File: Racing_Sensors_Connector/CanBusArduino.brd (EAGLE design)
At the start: 48.3 x 41.9 mm, 21 parts, among them U1 328P, Y1 16MHz

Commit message: Redesign PCB slightly
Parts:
- C1, C2: device SparkFun-Capacitors:0402 -> SparkFun-Capacitors:0603
- moved CANH/L 3.59 mm to (5.59, 36.2)
- moved PWR 3.59 mm to (5.59, 6.99)
- moved ADC0/1 3.26 mm to (5.59, 30.4)
- moved DIO 3.26 mm to (5.59, 12.8)
- moved ADC2/3 3.07 mm to (5.59, 24.5)
- moved ADC4/5 3.07 mm to (5.59, 18.7)
- turned R1 to 270 degrees
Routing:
- net RS: track 106.5 -> 100.8 mm
- net VCC: track 79.0 -> 73.5 mm
- net CANL: track 45.9 -> 41.0 mm
- net A3: track 19.1 -> 14.8 mm
- net CANH: track 41.5 -> 37.6 mm
- net D3: track 21.7 -> 18.1 mm
- net D4: track 38.0 -> 34.5 mm
- net A5: track 10.5 -> 7.26 mm
- net A4: track 14.1 -> 11.0 mm
- net A2: track 22.7 -> 20.0 mm
- net A1: track 27.1 -> 24.7 mm
- net A0: track 31.5 -> 29.3 mm
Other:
- board size 48.3 x 41.9 mm -> 48.3 x 43.2 mm

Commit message: Start redesign
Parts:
- removed C1, C2: 0.1uF, SparkFun-Capacitors:0603
- removed CAN_COMM: MCP2515, SparkFun-IC-Comms:DIP18
- removed CAP_2515_OSC1, CAP_2515_OSC2: 22pF, SparkFun-Capacitors:0603
- removed DIO: (no value), SparkFun-Connectors:MOLEX-1X2
- removed R1: 10k, SparkFun-Resistors:0603
- removed U1: 328P, SparkFun-IC-Microcontroller:DIP28
- removed Y1: 16MHz, SparkFun-Clocks:HC49US
- added ADC6/7, CANH/L2, I2C, TX/RX: (no value), SparkFun-Connectors:MOLEX-1X2
- added BYP1, BYP2: 0.1uF, SparkFun-Capacitors:0603
- added COSC1, COSC2: 22pF, SparkFun-Capacitors:0603
- added ISP: (no value), SparkFun-Connectors:2X3
- added OSC: 16MHz, SparkFun-Clocks:HC49US
- added RST_PULLUP, SD_PULLUP: 10k, SparkFun-Resistors:0603
- added U2: SPARKFUN_USD-SOCKETSMD, microSD-Breakout-v14:SPARKFUN_MICRO-SD-SOCKET-PP
- added U3: AT90CAN128-16AI, _hhn_at90can32_64_128_v2:TQFP64-0.8MM
- PRGM: value 455-1750-1-ND -> (none)
- moved PWR 37.5 mm to (43.0, 9.91), turned to 90 degrees
- moved R_2551_RS 7.62 mm to (30.5, 33.0)
- renumbered CANH/L to CANH/L1
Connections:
- removed net CAN_CS: CAN_COMM.16, U1.16
- removed net CAN_INT: CAN_COMM.12, U1.4
- removed net D3: DIO.2, U1.5
- removed net D4: DIO.1, U1.11
- removed net RS: CAN_COMM.17, PRGM.3, R1.2, U1.1
- new net A6: ADC6/7.1, U3.55
- new net A7: ADC6/7.2, U3.54
- new net RESET: ISP.5, PRGM.3, RST_PULLUP.1, U3.20
- new net RX1: TX/RX.2, U3.27
- new net SCL: I2C.2, U3.25
- new net SDA: I2C.1, U3.26
- new net SD_CD: SD_PULLUP.1, U2.CD2, U3.44
- new net SD_CS: U2.2, U3.45
- new net TX1: TX/RX.1, U3.28
- net A0: now also U3.61; no longer U1.23
- net A1: now also U3.60; no longer U1.24
- net A2: now also U3.59; no longer U1.25
- net A3: now also U3.58; no longer U1.26
- net A4: now also U3.57; no longer U1.27
- net A5: now also U3.56; no longer U1.28
- net CANH: now also CANH/L2.2
- net CANL: now also CANH/L2.1
- net CAN_RXD: now also U3.31; no longer CAN_COMM.2
- net CAN_TXD: now also U3.30; no longer CAN_COMM.1
- net GND: now also BYP1.2, BYP2.2, COSC1.2, COSC2.2, ISP.6, U2.6, U2.GND1, U2.GND2, U3.22, U3.53, U3.63; no longer C1.2, C2.2, CAN_COMM.9, CAP_2515_OSC1.2, CAP_2515_OSC2.2, U1.22, U1.8
- net MISO: now also ISP.1, U2.7, U3.13; no longer CAN_COMM.15, U1.18
- net MOSI: now also ISP.4, U2.3, U3.12; no longer CAN_COMM.14, U1.17
- net OSC1: now also COSC1.1, OSC.2, U3.24; no longer CAN_COMM.8, CAP_2515_OSC1.1, Y1.2
- net OSC2: now also COSC2.1, OSC.1, U3.23; no longer CAN_COMM.7, CAP_2515_OSC2.1, Y1.1
- net RX: now also U3.2; no longer U1.2
- net SCK: now also ISP.3, U2.5, U3.11; no longer CAN_COMM.13, U1.19
- net TX: now also U3.3; no longer U1.3
- net VCC: now also BYP1.1, BYP2.1, ISP.2, RST_PULLUP.2, SD_PULLUP.2, U2.4, U3.21, U3.52, U3.64; no longer C1.1, C2.1, CAN_COMM.18, R1.1, U1.20, U1.7
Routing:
- net RS: track 100.8 -> 0.00 mm
- net CAN_INT: track 75.8 -> 0.00 mm
- net RESET: track 0.00 -> 61.6 mm, vias 0 -> 1
- net CAN_CS: track 45.1 -> 0.00 mm
- net VCC: track 73.5 -> 117.6 mm, vias 0 -> 3
- net D4: track 34.5 -> 0.00 mm
- net A7: track 0.00 -> 32.0 mm, vias 0 -> 2
- net RX: track 3.81 -> 33.3 mm
- net RX1: track 0.00 -> 27.4 mm
- net A6: track 0.00 -> 26.5 mm, vias 0 -> 2
- net SCK: track 32.6 -> 56.3 mm, vias 0 -> 1
- net SCL: track 0.00 -> 22.7 mm
- net TX1: track 0.00 -> 20.6 mm
- net SDA: track 0.00 -> 20.5 mm, vias 0 -> 1
- net TX: track 3.81 -> 22.7 mm, vias 0 -> 1
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
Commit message: Before SD fix
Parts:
- removed CAN_INTERFACE: MCP2551-I/P, can_transceiver:DIP254P762X432-8
- removed R_2551_RS: 4.7k, SparkFun-Resistors:0603
- added IFACE: MCP2561-E/SN, Volks73-MicrochipTechnology:SOIC-8
- moved ISP 31.8 mm to (30.5, 2.54)
- moved I2C 30.7 mm to (34.3, 17.8), turned to 90 degrees
- moved BYP2 25.5 mm to (24.1, 5.08)
- moved ADC0/1 22.7 mm to (5.08, 7.62)
- moved PRGM 17.7 mm to (30.5, 7.62)
- moved COSC1 17.2 mm to (20.3, 38.1)
- moved COSC2 17.2 mm to (16.5, 38.1)
- moved OSC 17.2 mm to (7.62, 38.1)
- moved CANH/L2 16.9 mm to (34.3, 30.5)
- moved PWR 16.7 mm to (34.3, 24.1)
- moved BYP1 15.1 mm to (24.1, 26.7), turned to 180 degrees
- moved CAP_CANL 14.8 mm to (25.4, 30.5)
- moved R2 14.8 mm to (29.2, 30.5)
- moved ADC6/7 13.8 mm to (5.08, 26.7)
- moved U2 13.4 mm to (23.7, 16.8)
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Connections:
- removed net CI_RS: CAN_INTERFACE.8, R_2551_RS.2
- new net CAN_STBY: IFACE.8, U3.46
- net A0: now also ADC0/1.2; no longer ADC0/1.1
- net A1: now also ADC0/1.1; no longer ADC0/1.2
- net A2: now also ADC2/3.2; no longer ADC2/3.1
- net A3: now also ADC2/3.1; no longer ADC2/3.2
- net A4: now also ADC4/5.2; no longer ADC4/5.1
- net A5: now also ADC4/5.1; no longer ADC4/5.2
- net A6: now also ADC6/7.2; no longer ADC6/7.1
- net A7: now also ADC6/7.1; no longer ADC6/7.2
- net CANH: now also IFACE.7; no longer CAN_INTERFACE.7
- net CANL: now also IFACE.6; no longer CAN_INTERFACE.6
- net CAN_RXD: now also IFACE.4; no longer CAN_INTERFACE.4
- net CAN_TXD: now also IFACE.1; no longer CAN_INTERFACE.1
- net GND: now also IFACE.2; no longer CAN_INTERFACE.2, R_2551_RS.1
- net VCC: now also IFACE.3; no longer CAN_INTERFACE.3
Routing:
- net CAN_STBY: track 0.00 -> 49.1 mm
- net VCC: track 117.6 -> 69.6 mm, vias 3 -> 4
- net TX: track 22.7 -> 55.7 mm, vias 1 -> 0
- net RESET: track 61.6 -> 28.9 mm, vias 1 -> 0
- net RX: track 33.3 -> 60.8 mm
- net MISO: track 60.8 -> 34.2 mm
- net SCK: track 56.3 -> 34.2 mm
- net CANL: track 56.1 -> 36.2 mm, vias 0 -> 1
- net MOSI: track 53.6 -> 38.0 mm, vias 1 -> 3
- net A7: track 32.0 -> 17.2 mm, vias 2 -> 0
- net CAN_RXD: track 35.3 -> 24.7 mm, vias 0 -> 2
- net CANH: track 50.8 -> 40.3 mm
- net RX1: track 27.4 -> 17.8 mm
- net A6: track 26.5 -> 17.2 mm, vias 2 -> 0
- net CAN_TXD: track 24.8 -> 32.3 mm, vias 1 -> 2
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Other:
- board size 48.3 x 43.2 mm -> 39.4 x 40.6 mm
- board text added: "+"
- board text added: "7 6 5 4 3 2 1 0"
- board text added: "CAN Communicator WashU Racing 2018-19"
- board text added: "Connor Monahan"
- board text added: "H L"
- board text added: "L H"
- board text added: "RX1"
- board text added: "SCL"
- board text added: "SDA"
- board text added: "TX1"
- board text removed: "Design: Connor Monahan"
- board text removed: "Ethan Shry"
- board text removed: "WASHU RACING 2017-18"

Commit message: Teensy shield version
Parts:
- removed ADC0/1, ADC2/3, ADC4/5, ADC6/7, I2C, TX/RX: (no value), SparkFun-Connectors:MOLEX-1X2
- removed BYP2: 0.1uF, SparkFun-Capacitors:0603
- removed CAP_CANH, CAP_CANL: 560pF, SparkFun-Capacitors:0603
- removed COSC1, COSC2: 22pF, SparkFun-Capacitors:0603
- removed ISP: (no value), SparkFun-Connectors:2X3
- removed OSC: 16MHz, SparkFun-Clocks:HC49US
- removed PRGM: (no value), SparkFun-Connectors:1X03
- removed R2, R3: 100, SparkFun-Resistors:0603
- removed RST_PULLUP: 10k, SparkFun-Resistors:0603
- removed U3: AT90CAN128-16AI, _hhn_at90can32_64_128_v2:TQFP64-0.8MM
- added BT1: (no value), SparkFun-Batteries:BATTCON_20MM_4LEGS
- added CCANH, CCANL: 560pF, SparkFun-Capacitors:0603
- added RCANH, RCANL: 100, SparkFun-Resistors:0603
- added TEENSY: TEENSY_3.1-3.2_ALL_PINS, Teensy_3_and_LC_Series_Boards_v1.4:TEENSY_3.0-3.2&LC_ALL_PINS
- moved PWR 31.9 mm to (2.54, 26.7), turned to 270 degrees
- moved CANH/L2 25.3 mm to (10.2, 38.1), turned to 180 degrees
- moved IFACE 24.4 mm to (31.8, 12.7), flipped to the bottom
- moved BYP1 20.5 mm to (31.8, 7.62), flipped to the bottom
- moved U2 17.5 mm to (6.22, 16.0), flipped to the top
- moved SD_PULLUP 15.9 mm to (12.7, 19.1), turned to 0 degrees
- moved CANH/L1 2.54 mm to (2.54, 33.0)
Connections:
- removed net A4: ADC4/5.2, U3.57
- removed net A5: ADC4/5.1, U3.56
- removed net OSC1: COSC1.1, OSC.2, U3.24
- removed net OSC2: COSC2.1, OSC.1, U3.23
- removed net RESET: ISP.5, PRGM.3, RST_PULLUP.1, U3.20
- removed net RX: PRGM.1, U3.2
- removed net TX: PRGM.2, U3.3
- new net 3.3V: SD_PULLUP.2, TEENSY.3.3V, TEENSY.3.3V1, U2.4
- new net 3V: BT1.POSITIVE@1, BT1.POSITIVE@2, BT1.POSITIVE@3, BT1.POSITIVE@4, TEENSY.VBAT
- new net A8: TEENSY.22/A8
- new net A9: TEENSY.23/A9
- new net AREF: TEENSY.AREF
- new net VUSB: TEENSY.VUSB
- net A0: now also TEENSY.14/A0; no longer ADC0/1.2, U3.61
- net A1: now also TEENSY.15/A1; no longer ADC0/1.1, U3.60
- net A2: now also TEENSY.16/A2; no longer ADC2/3.2, U3.59
- net A3: now also TEENSY.17/A3; no longer ADC2/3.1, U3.58
- net A6: now also TEENSY.20/A6; no longer ADC6/7.2, U3.55
- net A7: now also TEENSY.21/A7; no longer ADC6/7.1, U3.54
- net CANH: now also RCANH.2; no longer R3.2
- net CANL: now also RCANL.2; no longer R2.2
- net CAN_RXD: now also TEENSY.4; no longer U3.31
- net CAN_STBY: now also TEENSY.5; no longer U3.46
- net CAN_TXD: now also TEENSY.3; no longer U3.30
- net GND: now also BT1.NEGATIVE, CCANH.2, CCANL.1, TEENSY.AGND, TEENSY.GND, TEENSY.GND1; no longer BYP2.2, CAP_CANH.2, CAP_CANL.1, COSC1.2, COSC2.2, ISP.6, U3.22, U3.53, U3.63
- net MISO: now also TEENSY.12; no longer ISP.1, U3.13
- net MOSI: now also TEENSY.11; no longer ISP.4, U3.12
- net N$6: now also CCANL.2, RCANL.1; no longer CAP_CANL.2, R2.1
- net N$7: now also CCANH.1, RCANH.1; no longer CAP_CANH.1, R3.1
- net RX1: now also TEENSY.0; no longer TX/RX.2, U3.27
- net SCK: now also TEENSY.13; no longer ISP.3, U3.11
- net SCL: now also TEENSY.19/A5; no longer I2C.2, U3.25
- net SDA: now also TEENSY.18/A4; no longer I2C.1, U3.26
- net SD_CD: now also TEENSY.7; no longer U3.44
- net SD_CS: now also TEENSY.6; no longer U3.45
- net TX1: now also TEENSY.1; no longer TX/RX.1, U3.28
- net VCC: now also TEENSY.VIN; no longer BYP2.1, ISP.2, RST_PULLUP.2, SD_PULLUP.2, U2.4, U3.21, U3.52, U3.64
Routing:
- net 3V: track 0.00 -> 62.1 mm, vias 0 -> 3
- net RX: track 60.8 -> 0.00 mm
- net TX: track 55.7 -> 0.00 mm
- net 3.3V: track 0.00 -> 54.3 mm
- net CAN_STBY: track 49.1 -> 4.90 mm
- net OSC2: track 42.4 -> 0.00 mm, vias 2 -> 0
- net OSC1: track 41.0 -> 0.00 mm, vias 2 -> 0
- net RESET: track 28.9 -> 0.00 mm
- net CAN_TXD: track 32.3 -> 5.04 mm, vias 2 -> 0
- net A0: track 23.5 -> 0.00 mm, vias 1 -> 0
- net SCL: track 22.2 -> 0.00 mm, vias 1 -> 0
- net A1: track 21.6 -> 0.00 mm, vias 1 -> 0
- net A3: track 21.4 -> 0.00 mm
- net MISO: track 34.2 -> 54.1 mm, vias 1 -> 0
- net SDA: track 19.7 -> 0.00 mm, vias 1 -> 0
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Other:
- board text added: "CR2032"
- board text added: "Install Teensy 3.2 on top of this text"
- board text added: "L H 5V GND"
- board text removed: "+"
- board text removed: "7 6 5 4 3 2 1 0"
- board text removed: "L H"
- board text removed: "RX1"
- board text removed: "SCL"
- board text removed: "SDA"
- board text removed: "TX1"

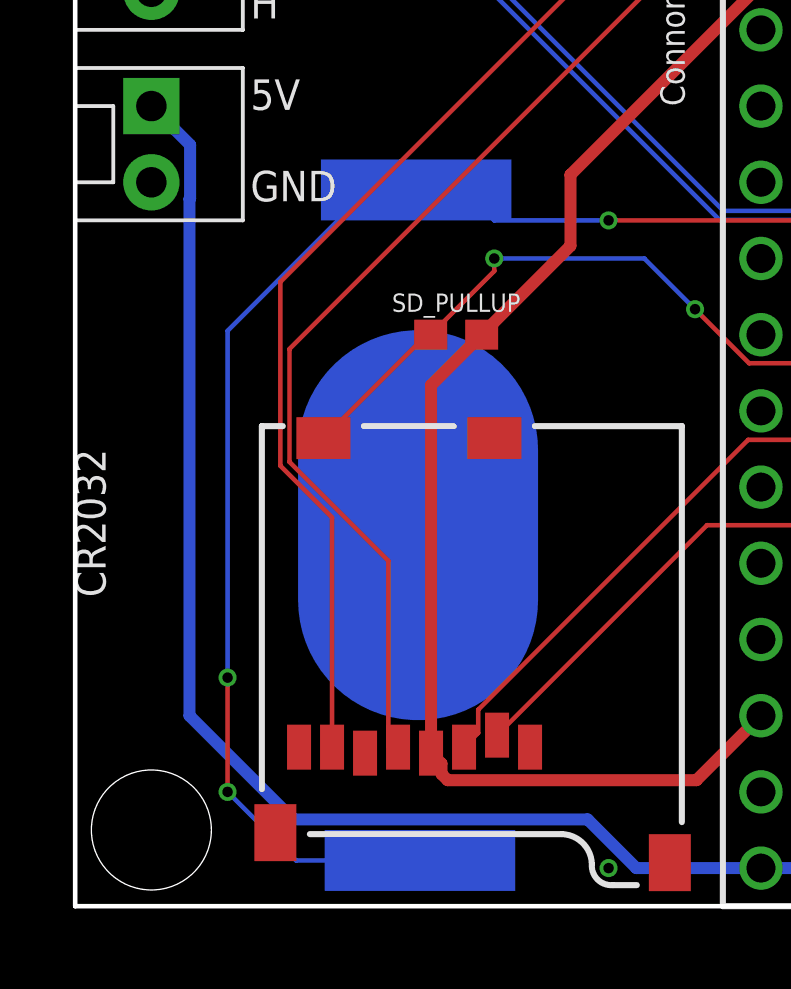
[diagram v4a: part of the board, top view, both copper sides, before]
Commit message: Make the battery face the right way
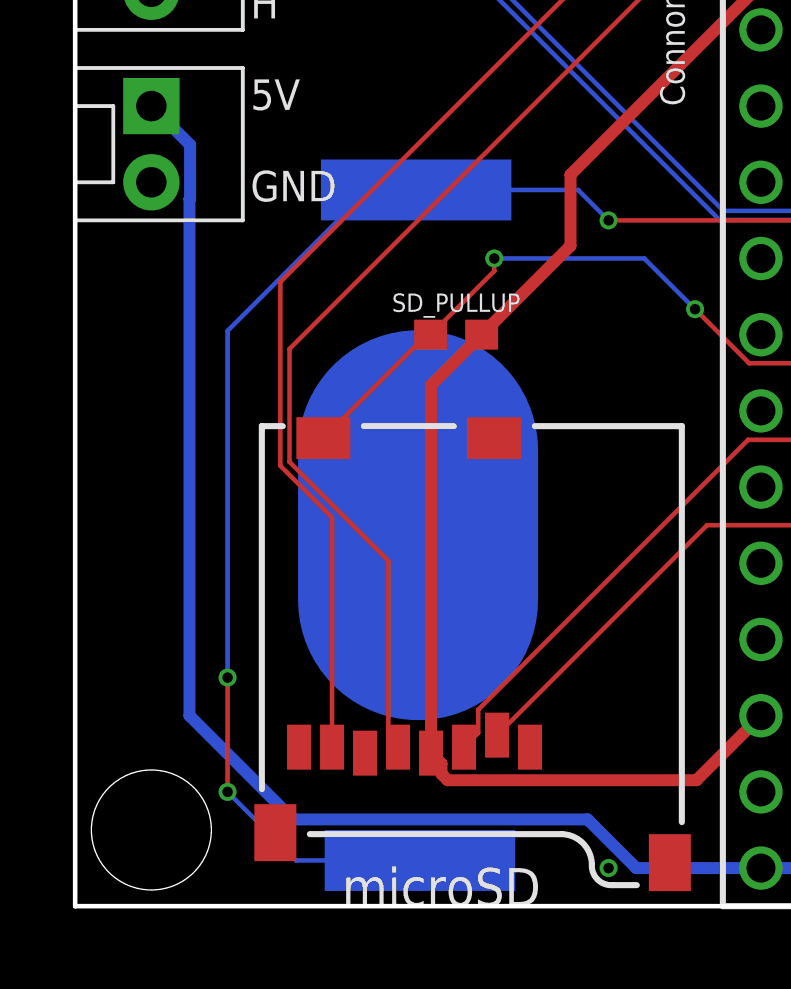
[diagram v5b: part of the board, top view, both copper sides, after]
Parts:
- turned BT1 to 90 degrees
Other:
- board text added: "microSD"
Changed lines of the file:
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@@
 <text x="33.02" y="11.43" size="1.778" layer="21" rot="R90">Install Teensy 3.2
 on top of this text</text>
-<text x="0" y="15.24" size="1.016" layer="21" rot="R270">CR2032</text>
+<text x="1.27" y="15.24" size="1.016" layer="22" rot="MR270">CR2032</text>
 <hole x="2.54" y="2.54" drill="4"/>
 <hole x="2.54" y="38.1" drill="4"/>
@@
 GND</text>
 <text x="6.985" y="33.782" size="1.016" layer="21" distance="200">H      L</text>
+<text x="8.89" y="0" size="1.27" layer="21">microSD</text>
 </plain>
 <attributes>
@@
 <attribute name="VALUE" x="34.29" y="31.75" size="1.27" layer="27" font="vector" rot="R180"/>
 </element>
-<element name="BT1" library="SparkFun-Batteries" library_urn="urn:adsk.eagle:library:508" package="BATTCON_20MM_4LEGS" package3d_urn="urn:adsk.eagle:package:37217/1" value="" x="11.43" y="12.7" smashed="yes" rot="MR270">
-<attribute name="NAME" x="3.937" y="12.7" size="0.6096" layer="26" font="vector" ratio="20" rot="MR270" align="bottom-center"/>
-<attribute name="PROD_ID" value="BATT-10373" x="11.43" y="12.7" size="1.778" layer="28" rot="MR270" display="off"/>
-<attribute name="SF_SKU" value="PRT-11892" x="11.43" y="12.7" size="1.778" layer="28" rot="MR270" display="off"/>
-<attribute name="VALUE" x="4.318" y="12.7" size="0.6096" layer="28" font="vector" ratio="20" rot="MR270" align="top-center"/>
+<element name="BT1" library="SparkFun-Batteries" library_urn="urn:adsk.eagle:library:508" package="BATTCON_20MM_4LEGS" package3d_urn="urn:adsk.eagle:package:37217/1" value="" x="11.43" y="12.7" smashed="yes" rot="MR90">
+<attribute name="NAME" x="18.923" y="12.7" size="0.6096" layer="26" font="vector" ratio="20" rot="MR90" align="bottom-center"/>
+<attribute name="PROD_ID" value="BATT-10373" x="11.43" y="12.7" size="1.778" layer="28" rot="MR90" display="off"/>
+<attribute name="SF_SKU" value="PRT-11892" x="11.43" y="12.7" size="1.778" layer="28" rot="MR90" display="off"/>
+<attribute name="VALUE" x="18.542" y="12.7" size="0.6096" layer="28" font="vector" ratio="20" rot="MR90" align="top-center"/>
 </element>
 </elements>
@@
 <wire x1="24.13" y1="22.86" x2="17.78" y2="22.86" width="0.1524" layer="1"/>
 <via x="17.78" y="22.86" extent="1-16" drill="0.35"/>
-<wire x1="17.78" y1="22.86" x2="13.97" y2="22.86" width="0.1524" layer="16"/>
-<wire x1="13.97" y1="22.86" x2="12.954" y2="23.876" width="0.1524" layer="16"/>
-<wire x1="9.779" y1="23.876" x2="12.446" y2="23.876" width="0.1524" layer="16"/>
-<wire x1="12.446" y1="23.876" x2="12.7" y2="24.13" width="0.1524" layer="16"/>
-<wire x1="12.7" y1="24.13" x2="12.954" y2="23.876" width="0.1524" layer="16"/>
-<wire x1="9.779" y1="23.876" x2="5.08" y2="19.177" width="0.1524" layer="16"/>
+<via x="5.08" y="7.62" extent="1-16" drill="0.35"/>
 <wire x1="5.08" y1="19.177" x2="5.08" y2="7.62" width="0.1524" layer="16"/>
-<via x="5.08" y="7.62" extent="1-16" drill="0.35"/>
 <wire x1="5.08" y1="7.62" x2="5.08" y2="3.81" width="0.1524" layer="1"/>
 <via x="5.08" y="3.81" extent="1-16" drill="0.35"/>
@@
 <wire x1="7.366" y1="1.524" x2="9.906" y2="1.524" width="0.1524" layer="16"/>
 <wire x1="9.906" y1="1.524" x2="13.081" y2="1.524" width="0.1524" layer="16"/>
+<wire x1="5.08" y1="19.177" x2="9.779" y2="23.876" width="0.1524" layer="16"/>
+<wire x1="9.779" y1="23.876" x2="12.954" y2="23.876" width="0.1524" layer="16"/>
+<wire x1="12.954" y1="23.876" x2="16.764" y2="23.876" width="0.1524" layer="16"/>
+<wire x1="16.764" y1="23.876" x2="17.78" y2="22.86" width="0.1524" layer="16"/>
 </signal>
 <signal name="3.3V">
